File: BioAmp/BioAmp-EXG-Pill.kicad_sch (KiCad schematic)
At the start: 30 parts, among them IC1 MCP3221A4T-E_OT, J1 Conn_01x03_Pin, J2 Conn_01x04_Pin, J3 Conn_01x04_Pin, U1 Amp, U2 LOGO_UDLABS, U3 TPD1E05U06DPY, U4 TPD1E05U06DPY, U5 TPD1E05U06DPY, U6 TPD1E05U06DPY, U7 TPD1E05U06DPY, U8 TPD1E05U06DPY

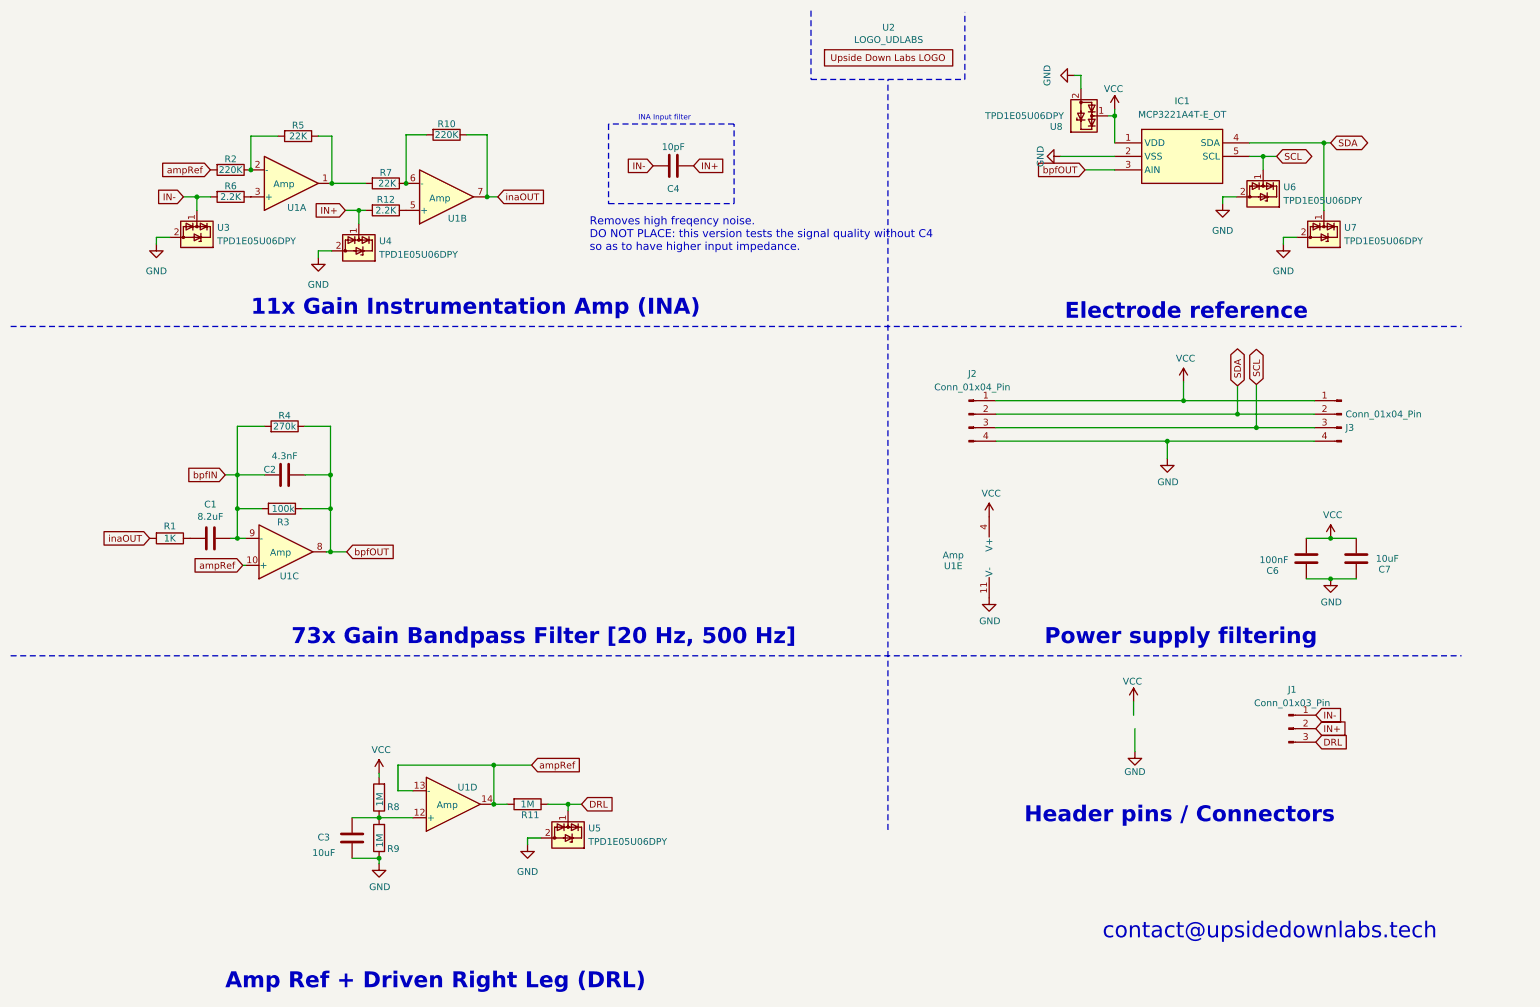
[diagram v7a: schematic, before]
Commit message: Added new ADC and cleaned up ESD protection
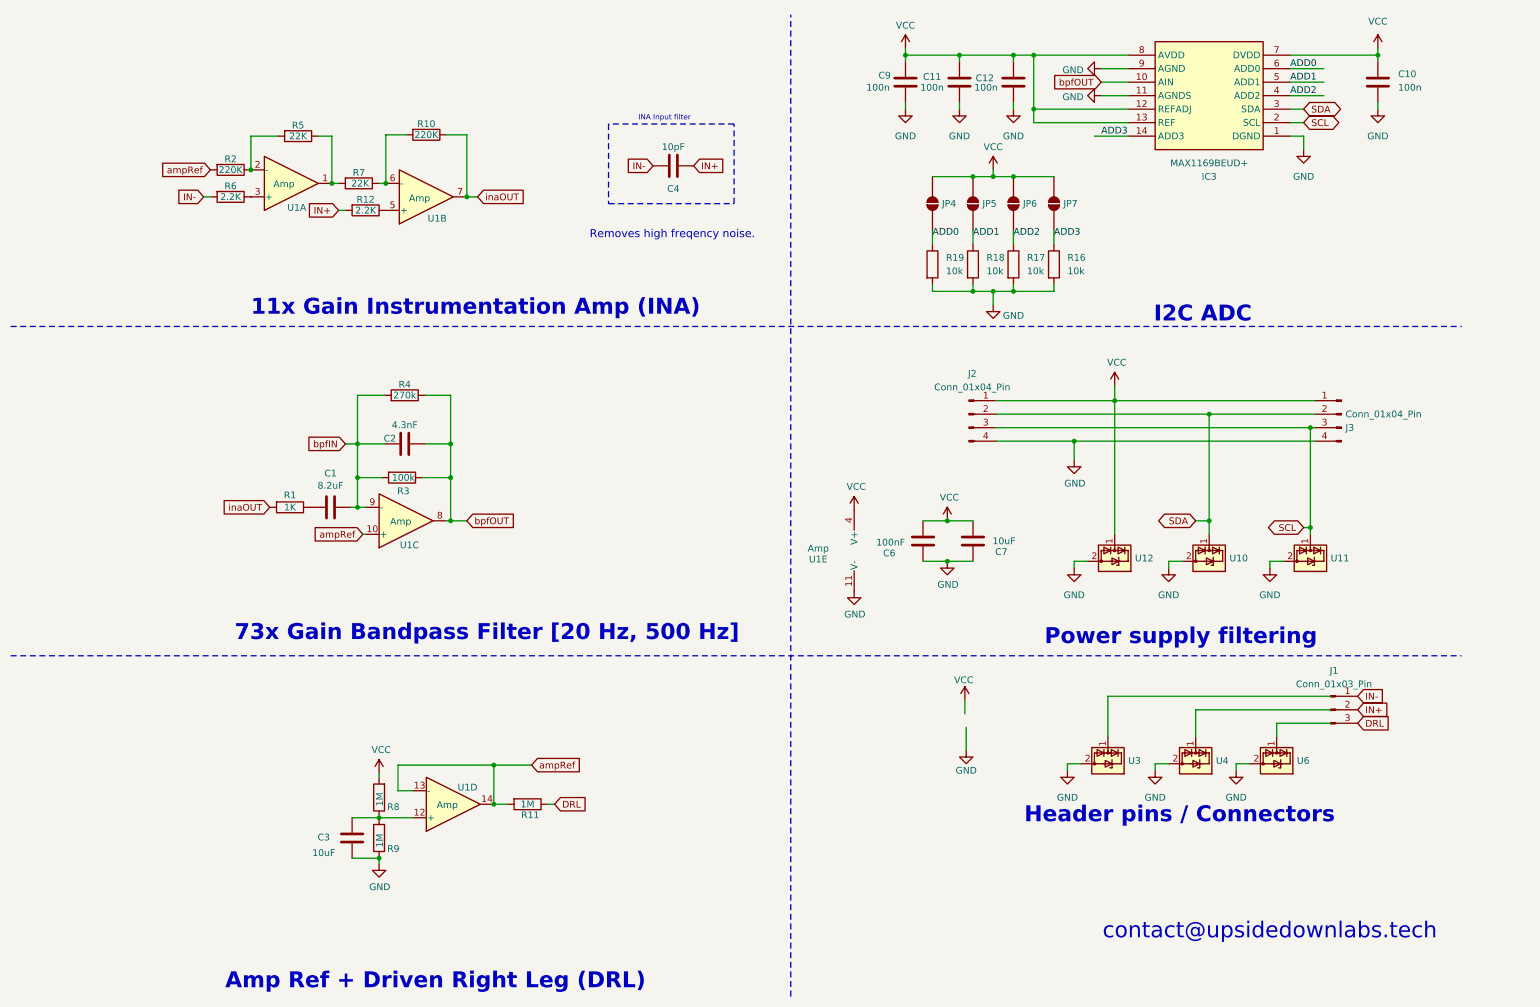
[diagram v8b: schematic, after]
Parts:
- removed IC1: MCP3221A4T-E_OT, ADC:SOT95P280X145-5N, symbol MCP3221A4T-E_OT:MCP3221A4T-E_OT
- removed U2: LOGO_UDLABS, udlabs:EXG, symbol BioAmp-EXG-Pill-rescue:LOGO_UDLABS-udlabs
- removed U5, U7, U8: TPD1E05U06DPY, Package_SON:Texas_DPY0002A_0.6x1mm_P0.65mm, symbol Power_Protection:TPD1E05U06DPY
- added C10, C11, C12, C9: 100n, Capacitor_SMD:C_0603_1608Metric_Pad1.08x0.95mm_HandSolder, symbol Device:C
- added IC3: MAX1169BEUD+, MAX1169:SOP65P640X110-14N, symbol MAX1169:MAX1169BEUD+
- added JP4, JP5, JP6, JP7: SolderJumper_2_Open, Jumper:SolderJumper-2_P1.3mm_Open_RoundedPad1.0x1.5mm, symbol Jumper:SolderJumper_2_Open
- added R16, R17, R18, R19: 10k, Resistor_SMD:R_0402_1005Metric, symbol Device:R
- added U10, U11, U12: TPD1E05U06DPY, Package_SON:Texas_DPY0002A_0.6x1mm_P0.65mm, symbol Power_Protection:TPD1E05U06DPY
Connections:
- net GND: now also C10.1, C11.1, C12.1, C9.1, IC3.1 (DGND), IC3.11 (AGNDS), IC3.9 (AGND), R16.2, R17.2, R18.2, R19.2, U10.2 (GND), U11.2 (GND), U12.2 (GND)
- net IN+: no longer U4.1 (I/O)
- net IN-: no longer U3.1 (I/O)
- net SCL: now also IC3.2 (SCL), U11.1 (I/O); no longer U6.1 (I/O)
- net SDA: now also IC3.3 (SDA), U10.1 (I/O)
- net VCC: now also C10.2, C11.2, C12.2, C9.2, IC3.12 (REFADJ), IC3.13 (REF), IC3.7 (DVDD), IC3.8 (AVDD), JP4.2 (B), JP5.2 (B), JP6.2 (B), JP7.2 (B), U12.1 (I/O)
- net bpfOUT: now also IC3.10 (AIN)
- new net ADD0: IC3.6 (ADD0), JP4.1 (A), R19.1
- new net ADD1: IC3.5 (ADD1), JP5.1 (A), R18.1
- new net ADD2: IC3.4 (ADD2), JP6.1 (A), R17.1
- new net ADD3: IC3.14 (ADD3), JP7.1 (A), R16.1
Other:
- note added: "I2C ADC"
- note added: "Removes high freqency noise."
- note removed: "Electrode reference"
- note removed: "Removes high freqency noise. DO NOT PLACE: this version tests the signal quality without C4 so as to have higher input impedance."
- moved on the sheet: C1, C2, C6, C7, J1, R1, R10, R12, R3, R4, R7, U1B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
